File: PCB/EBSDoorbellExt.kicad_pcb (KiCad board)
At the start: 2 copper layers, 65.8 x 49 mm, 41 parts, among them P1 AC in, P2 Doorbell, Q1 BC846C, SW1 Power, SW2 Test, U1 LM7809ACT, U2 LM555N

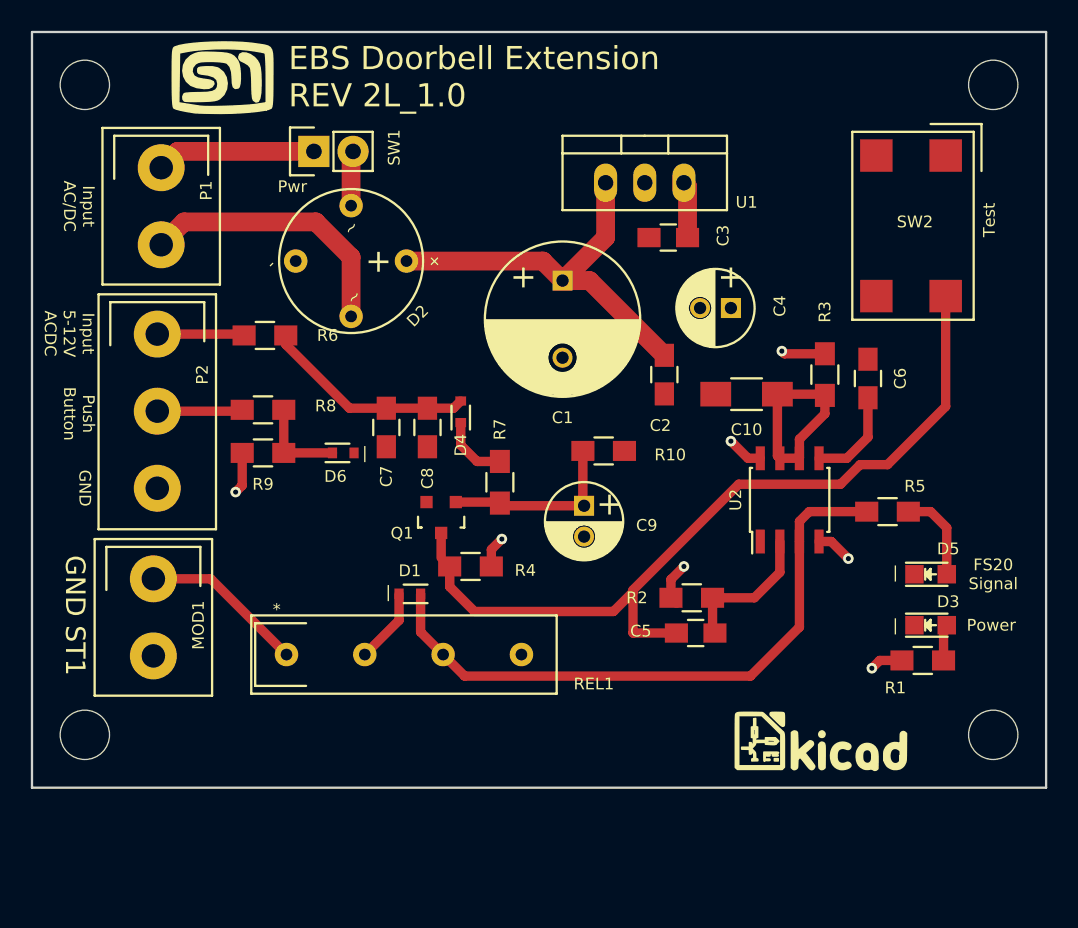
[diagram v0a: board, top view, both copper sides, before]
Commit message: Updated the layout to include the heatsink
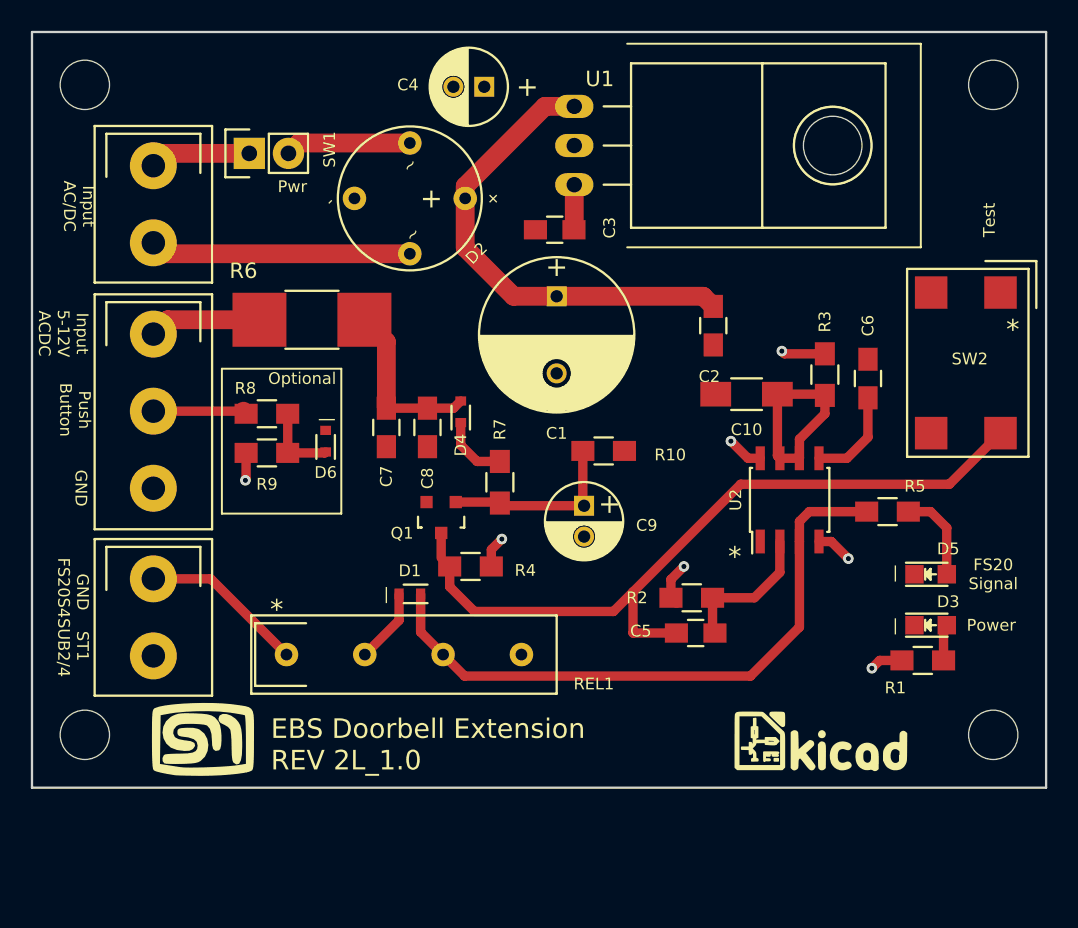
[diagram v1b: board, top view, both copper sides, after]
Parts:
- added REF**: 274_2AB, EBSDoorbellExt-Footprints:274_2AB, F.Cu at (178.3, 74.8)
- R6: footprint Resistors_SMD:R_0805_HandSoldering -> Resistors_SMD:R_1812_HandSoldering
- U1: footprint TO_SOT_Packages_THT:TO-220_Neutral123_Vertical -> TO_SOT_Packages_THT:TO-220_Neutral123_Horizontal
- moved G*** 42.9 mm to (141.2, 113.3)
- moved C4 21.5 mm to (159.5, 71.0)
- moved SW2 9.57 mm to (190.8, 88.9)
- moved C3 7.38 mm to (164.1, 80.3)
- moved D2 5.57 mm to (154.7, 78.2)
- moved U1 5.17 mm to (165.4, 74.8), turned to 270 degrees
- moved C2 4.49 mm to (174.4, 86.5)
- moved SW1 4.19 mm to (144.3, 75.3)
- moved R6 3.21 mm to (148.3, 86.1)
- moved D6 1.37 mm to (149.2, 94.0), turned to 270 degrees
- moved C1 1.09 mm to (164.2, 84.6)
- moved P1 0.52 mm to (138.0, 78.6)
- moved R8 0.36 mm to (145.4, 92.2)
- moved P2 0.25 mm to (138.0, 92.1)
- moved R9 0.25 mm to (145.4, 94.7)
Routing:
- net Net-(D2-Pad2): track 3.57 -> 8.15 mm
- net /~Trigger: track 54.0 -> 49.6 mm
- net Net-(C1-Pad1): track 26.8 -> 30.9 mm
- net /In1: track 10.3 -> 6.56 mm
- net Net-(C7-Pad1): track 13.8 -> 11.3 mm
- net /Vcc: track 21.1 -> 19.4 mm
- net Net-(P2-Pad1): track 5.67 -> 7.27 mm
- net Net-(D6-Pad1): track 5.95 -> 5.03 mm
- net /In2: track 17.7 -> 16.9 mm
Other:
- board text added: "*"
- board text added: "GND ST1 FS20S4SUB2/4"
- board text added: "Optional"
- board text removed: "GND ST1"

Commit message: Added some test points and moved the LEDs help with the casing
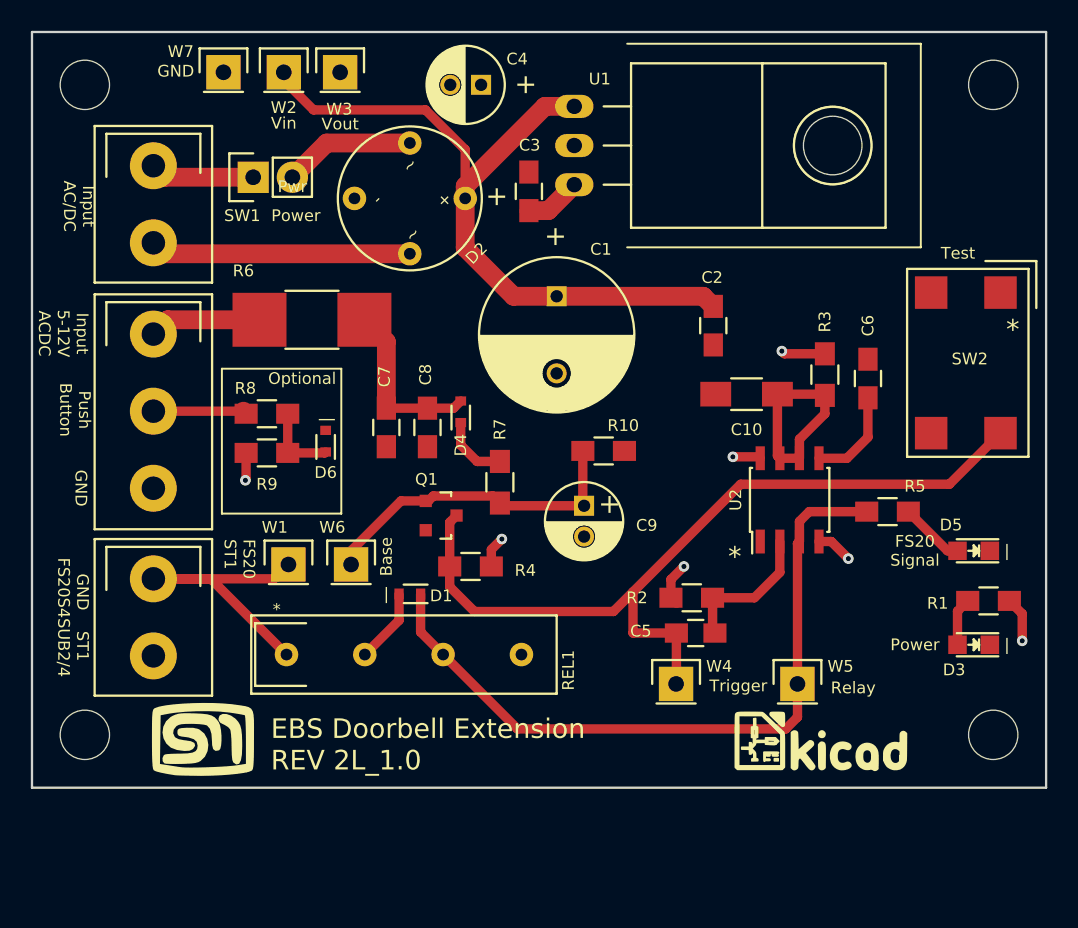
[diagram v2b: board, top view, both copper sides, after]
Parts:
- added W1: FS20_ST1, Pin_Headers:Pin_Header_Straight_1x01, F.Cu at (146.8, 102.0)
- added W2: Vin, Pin_Headers:Pin_Header_Straight_1x01, F.Cu at (146.5, 70.1)
- added W3: Vout, Pin_Headers:Pin_Header_Straight_1x01, F.Cu at (150.2, 70.1)
- added W4: Trigger, Pin_Headers:Pin_Header_Straight_1x01, F.Cu at (172.0, 109.7)
- added W5: Relay, Pin_Headers:Pin_Header_Straight_1x01, F.Cu at (179.8, 109.7)
- added W6: Base, Pin_Headers:Pin_Header_Straight_1x01, F.Cu at (150.9, 102.0)
- added W7: GND, Pin_Headers:Pin_Header_Straight_1x01, F.Cu at (142.6, 70.1)
- U1: value LM7809ACT -> LM7812CT
- moved R1 5.75 mm to (192.2, 104.3), turned to 180 degrees
- moved D5 3.18 mm to (191.3, 101.1), turned to 180 degrees
- moved D3 3.07 mm to (191.3, 107.2), turned to 180 degrees
- moved C3 3.00 mm to (162.4, 77.8), turned to 90 degrees
- moved SW1 1.57 mm to (144.5, 76.9)
- moved C4 0.24 mm to (159.3, 70.9)
- moved Q1 0.13 mm to (156.7, 98.8), turned to 270 degrees
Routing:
- net Net-(C1-Pad1): track 30.9 -> 48.2 mm
- net Net-(C9-Pad1): track 12.0 -> 21.4 mm
- net Net-(MOD1-Pad1): track 10.7 -> 19.8 mm
- net /FS20_Sig: track 41.0 -> 47.2 mm
- net /~Trigger: track 49.6 -> 54.8 mm
- net Net-(D5-Pad2): track 5.94 -> 4.24 mm
- net /Vcc: track 19.4 -> 20.4 mm
- net Net-(D3-Pad2): track 2.37 -> 3.12 mm
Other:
- rule pad_to_mask_clearance: 0.2 -> 0
- board text added: "Base"
- board text added: "FS20 ST1"
- board text added: "Relay"
- board text added: "Trigger"
- board text added: "Vin"
- board text added: "Vout"

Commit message: Changed the layout to use an Optocoupler instead of a relay and generated Gerbers
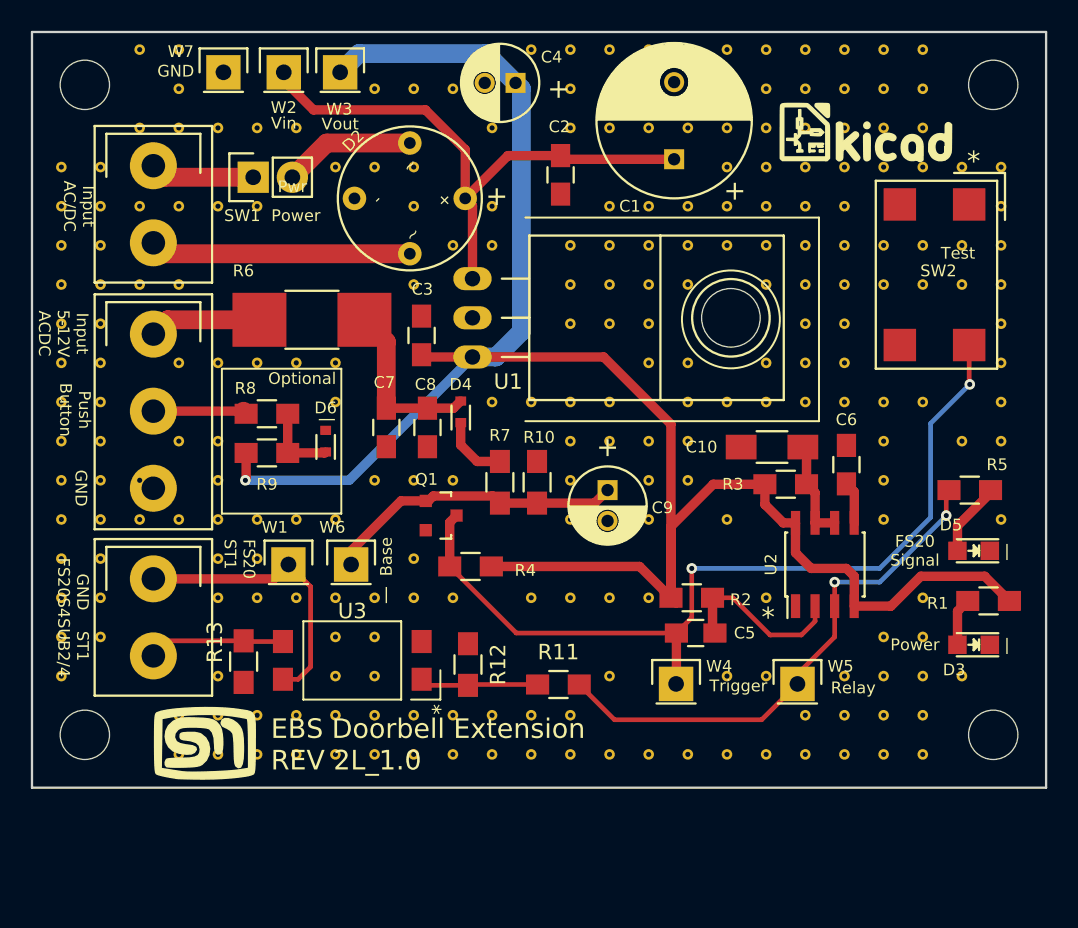
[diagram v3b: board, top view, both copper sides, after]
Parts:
- removed D1: 1N4148W, Diodes_SMD:SOD-523
- removed REL1: MES1A12, EBSDoorbellExt-Footprints:MES1A12
- added R11: 1kΩ, Resistors_SMD:R_0805_HandSoldering, F.Cu at (164.3, 109.8)
- added R12: 10kΩ, Resistors_SMD:R_0805_HandSoldering, F.Cu at (158.5, 108.5)
- added R13: NOPOP, Resistors_SMD:R_0805_HandSoldering, F.Cu at (143.9, 108.3)
- added ST**1012: Stitch_VIA, EBSDoorbellExt-Footprints:Stitch_VIA, F.Cu at (154.9, 96.5)
- added ST**1014: Stitch_VIA, EBSDoorbellExt-Footprints:Stitch_VIA, F.Cu at (154.9, 101.6)
- added ST**1015: Stitch_VIA, EBSDoorbellExt-Footprints:Stitch_VIA, F.Cu at (154.9, 104.1)
- added ST**1018: Stitch_VIA, EBSDoorbellExt-Footprints:Stitch_VIA, F.Cu at (154.9, 111.8)
- added ST**1019: Stitch_VIA, EBSDoorbellExt-Footprints:Stitch_VIA, F.Cu at (154.9, 114.3)
- added ST**102: Stitch_VIA, EBSDoorbellExt-Footprints:Stitch_VIA, F.Cu at (154.9, 71.1)
- added ST**104: Stitch_VIA, EBSDoorbellExt-Footprints:Stitch_VIA, F.Cu at (154.9, 76.2)
- added ST**105: Stitch_VIA, EBSDoorbellExt-Footprints:Stitch_VIA, F.Cu at (154.9, 78.7)
- added ST**107: Stitch_VIA, EBSDoorbellExt-Footprints:Stitch_VIA, F.Cu at (154.9, 83.8)
- added ST**110: Stitch_VIA, EBSDoorbellExt-Footprints:Stitch_VIA, F.Cu at (132.1, 91.4)
- added ST**111: Stitch_VIA, EBSDoorbellExt-Footprints:Stitch_VIA, F.Cu at (132.1, 94.0)
- added ST**1112: Stitch_VIA, EBSDoorbellExt-Footprints:Stitch_VIA, F.Cu at (157.5, 96.5)
- added ST**1115: Stitch_VIA, EBSDoorbellExt-Footprints:Stitch_VIA, F.Cu at (157.5, 104.1)
- added ST**1118: Stitch_VIA, EBSDoorbellExt-Footprints:Stitch_VIA, F.Cu at (157.5, 111.8)
- added ST**1119: Stitch_VIA, EBSDoorbellExt-Footprints:Stitch_VIA, F.Cu at (157.5, 114.3)
- added ST**112: Stitch_VIA, EBSDoorbellExt-Footprints:Stitch_VIA, F.Cu at (132.1, 96.5)
- added ST**112: Stitch_VIA, EBSDoorbellExt-Footprints:Stitch_VIA, F.Cu at (157.5, 71.1)
- added ST**113: Stitch_VIA, EBSDoorbellExt-Footprints:Stitch_VIA, F.Cu at (132.1, 99.1)
- added ST**114: Stitch_VIA, EBSDoorbellExt-Footprints:Stitch_VIA, F.Cu at (132.1, 101.6)
- added ST**115: Stitch_VIA, EBSDoorbellExt-Footprints:Stitch_VIA, F.Cu at (132.1, 104.1)
- added ST**116: Stitch_VIA, EBSDoorbellExt-Footprints:Stitch_VIA, F.Cu at (132.1, 106.7)
- added ST**116: Stitch_VIA, EBSDoorbellExt-Footprints:Stitch_VIA, F.Cu at (157.5, 81.3)
- added ST**117: Stitch_VIA, EBSDoorbellExt-Footprints:Stitch_VIA, F.Cu at (132.1, 109.2)
- added ST**1210: Stitch_VIA, EBSDoorbellExt-Footprints:Stitch_VIA, F.Cu at (160.0, 91.4)
- added ST**1218: Stitch_VIA, EBSDoorbellExt-Footprints:Stitch_VIA, F.Cu at (160.0, 111.8)
- added ST**1219: Stitch_VIA, EBSDoorbellExt-Footprints:Stitch_VIA, F.Cu at (160.0, 114.3)
- added ST**123: Stitch_VIA, EBSDoorbellExt-Footprints:Stitch_VIA, F.Cu at (160.0, 73.7)
- added ST**125: Stitch_VIA, EBSDoorbellExt-Footprints:Stitch_VIA, F.Cu at (160.0, 78.7)
- added ST**126: Stitch_VIA, EBSDoorbellExt-Footprints:Stitch_VIA, F.Cu at (160.0, 81.3)
- added ST**131: Stitch_VIA, EBSDoorbellExt-Footprints:Stitch_VIA, F.Cu at (162.6, 68.6)
- added ST**1310: Stitch_VIA, EBSDoorbellExt-Footprints:Stitch_VIA, F.Cu at (162.6, 91.4)
- added ST**1315: Stitch_VIA, EBSDoorbellExt-Footprints:Stitch_VIA, F.Cu at (162.6, 104.1)
- added ST**1318: Stitch_VIA, EBSDoorbellExt-Footprints:Stitch_VIA, F.Cu at (162.6, 111.8)
- added ST**1319: Stitch_VIA, EBSDoorbellExt-Footprints:Stitch_VIA, F.Cu at (162.6, 114.3)
- added ST**14: Stitch_VIA, EBSDoorbellExt-Footprints:Stitch_VIA, F.Cu at (132.1, 76.2)
- added ST**141: Stitch_VIA, EBSDoorbellExt-Footprints:Stitch_VIA, F.Cu at (165.1, 68.6)
- added ST**1410: Stitch_VIA, EBSDoorbellExt-Footprints:Stitch_VIA, F.Cu at (165.1, 91.4)
- added ST**1411: Stitch_VIA, EBSDoorbellExt-Footprints:Stitch_VIA, F.Cu at (165.1, 94.0)
- added ST**1412: Stitch_VIA, EBSDoorbellExt-Footprints:Stitch_VIA, F.Cu at (165.1, 96.5)
- added ST**1413: Stitch_VIA, EBSDoorbellExt-Footprints:Stitch_VIA, F.Cu at (165.1, 99.1)
- added ST**1415: Stitch_VIA, EBSDoorbellExt-Footprints:Stitch_VIA, F.Cu at (165.1, 104.1)
- added ST**1418: Stitch_VIA, EBSDoorbellExt-Footprints:Stitch_VIA, F.Cu at (165.1, 111.8)
- added ST**1419: Stitch_VIA, EBSDoorbellExt-Footprints:Stitch_VIA, F.Cu at (165.1, 114.3)
- added ST**142: Stitch_VIA, EBSDoorbellExt-Footprints:Stitch_VIA, F.Cu at (165.1, 71.1)
- added ST**143: Stitch_VIA, EBSDoorbellExt-Footprints:Stitch_VIA, F.Cu at (165.1, 73.7)
- added ST**146: Stitch_VIA, EBSDoorbellExt-Footprints:Stitch_VIA, F.Cu at (165.1, 81.3)
- added ST**147: Stitch_VIA, EBSDoorbellExt-Footprints:Stitch_VIA, F.Cu at (165.1, 83.8)
- added ST**148: Stitch_VIA, EBSDoorbellExt-Footprints:Stitch_VIA, F.Cu at (165.1, 86.4)
- added ST**15: Stitch_VIA, EBSDoorbellExt-Footprints:Stitch_VIA, F.Cu at (132.1, 78.7)
- added ST**151: Stitch_VIA, EBSDoorbellExt-Footprints:Stitch_VIA, F.Cu at (167.6, 68.6)
- added ST**1510: Stitch_VIA, EBSDoorbellExt-Footprints:Stitch_VIA, F.Cu at (167.6, 91.4)
- added ST**1511: Stitch_VIA, EBSDoorbellExt-Footprints:Stitch_VIA, F.Cu at (167.6, 94.0)
- added ST**1513: Stitch_VIA, EBSDoorbellExt-Footprints:Stitch_VIA, F.Cu at (167.6, 99.1)
- added ST**1515: Stitch_VIA, EBSDoorbellExt-Footprints:Stitch_VIA, F.Cu at (167.6, 104.1)
- added ST**1517: Stitch_VIA, EBSDoorbellExt-Footprints:Stitch_VIA, F.Cu at (167.6, 109.2)
- added ST**1519: Stitch_VIA, EBSDoorbellExt-Footprints:Stitch_VIA, F.Cu at (167.6, 114.3)
- added ST**152: Stitch_VIA, EBSDoorbellExt-Footprints:Stitch_VIA, F.Cu at (167.6, 71.1)
- added ST**153: Stitch_VIA, EBSDoorbellExt-Footprints:Stitch_VIA, F.Cu at (167.6, 73.7)
- added ST**155: Stitch_VIA, EBSDoorbellExt-Footprints:Stitch_VIA, F.Cu at (167.6, 78.7)
- added ST**156: Stitch_VIA, EBSDoorbellExt-Footprints:Stitch_VIA, F.Cu at (167.6, 81.3)
- added ST**157: Stitch_VIA, EBSDoorbellExt-Footprints:Stitch_VIA, F.Cu at (167.6, 83.8)
- added ST**158: Stitch_VIA, EBSDoorbellExt-Footprints:Stitch_VIA, F.Cu at (167.6, 86.4)
- added ST**16: Stitch_VIA, EBSDoorbellExt-Footprints:Stitch_VIA, F.Cu at (132.1, 81.3)
- added ST**161: Stitch_VIA, EBSDoorbellExt-Footprints:Stitch_VIA, F.Cu at (170.2, 68.6)
- added ST**1611: Stitch_VIA, EBSDoorbellExt-Footprints:Stitch_VIA, F.Cu at (170.2, 94.0)
- added ST**1612: Stitch_VIA, EBSDoorbellExt-Footprints:Stitch_VIA, F.Cu at (170.2, 96.5)
- added ST**1613: Stitch_VIA, EBSDoorbellExt-Footprints:Stitch_VIA, F.Cu at (170.2, 99.1)
- added ST**1615: Stitch_VIA, EBSDoorbellExt-Footprints:Stitch_VIA, F.Cu at (170.2, 104.1)
- added ST**1619: Stitch_VIA, EBSDoorbellExt-Footprints:Stitch_VIA, F.Cu at (170.2, 114.3)
- added ST**162: Stitch_VIA, EBSDoorbellExt-Footprints:Stitch_VIA, F.Cu at (170.2, 71.1)
- added ST**163: Stitch_VIA, EBSDoorbellExt-Footprints:Stitch_VIA, F.Cu at (170.2, 73.7)
- added ST**165: Stitch_VIA, EBSDoorbellExt-Footprints:Stitch_VIA, F.Cu at (170.2, 78.7)
- added ST**166: Stitch_VIA, EBSDoorbellExt-Footprints:Stitch_VIA, F.Cu at (170.2, 81.3)
- added ST**167: Stitch_VIA, EBSDoorbellExt-Footprints:Stitch_VIA, F.Cu at (170.2, 83.8)
- added ST**168: Stitch_VIA, EBSDoorbellExt-Footprints:Stitch_VIA, F.Cu at (170.2, 86.4)
- added ST**169: Stitch_VIA, EBSDoorbellExt-Footprints:Stitch_VIA, F.Cu at (170.2, 88.9)
- added ST**17: Stitch_VIA, EBSDoorbellExt-Footprints:Stitch_VIA, F.Cu at (132.1, 83.8)
- added ST**171: Stitch_VIA, EBSDoorbellExt-Footprints:Stitch_VIA, F.Cu at (172.7, 68.6)
- added ST**1710: Stitch_VIA, EBSDoorbellExt-Footprints:Stitch_VIA, F.Cu at (172.7, 91.4)
- added ST**1711: Stitch_VIA, EBSDoorbellExt-Footprints:Stitch_VIA, F.Cu at (172.7, 94.0)
- added ST**1712: Stitch_VIA, EBSDoorbellExt-Footprints:Stitch_VIA, F.Cu at (172.7, 96.5)
- added ST**1719: Stitch_VIA, EBSDoorbellExt-Footprints:Stitch_VIA, F.Cu at (172.7, 114.3)
- added ST**173: Stitch_VIA, EBSDoorbellExt-Footprints:Stitch_VIA, F.Cu at (172.7, 73.7)
- added ST**175: Stitch_VIA, EBSDoorbellExt-Footprints:Stitch_VIA, F.Cu at (172.7, 78.7)
- added ST**176: Stitch_VIA, EBSDoorbellExt-Footprints:Stitch_VIA, F.Cu at (172.7, 81.3)
- added ST**177: Stitch_VIA, EBSDoorbellExt-Footprints:Stitch_VIA, F.Cu at (172.7, 83.8)
- added ST**179: Stitch_VIA, EBSDoorbellExt-Footprints:Stitch_VIA, F.Cu at (172.7, 88.9)
- added ST**18: Stitch_VIA, EBSDoorbellExt-Footprints:Stitch_VIA, F.Cu at (132.1, 86.4)
- added ST**181: Stitch_VIA, EBSDoorbellExt-Footprints:Stitch_VIA, F.Cu at (175.3, 68.6)
- added ST**1810: Stitch_VIA, EBSDoorbellExt-Footprints:Stitch_VIA, F.Cu at (175.3, 91.4)
- added ST**1813: Stitch_VIA, EBSDoorbellExt-Footprints:Stitch_VIA, F.Cu at (175.3, 99.1)
- added ST**1817: Stitch_VIA, EBSDoorbellExt-Footprints:Stitch_VIA, F.Cu at (175.3, 109.2)
- added ST**1819: Stitch_VIA, EBSDoorbellExt-Footprints:Stitch_VIA, F.Cu at (175.3, 114.3)
- added ST**182: Stitch_VIA, EBSDoorbellExt-Footprints:Stitch_VIA, F.Cu at (175.3, 71.1)
- added ST**183: Stitch_VIA, EBSDoorbellExt-Footprints:Stitch_VIA, F.Cu at (175.3, 73.7)
- added ST**184: Stitch_VIA, EBSDoorbellExt-Footprints:Stitch_VIA, F.Cu at (175.3, 76.2)
- added ST**185: Stitch_VIA, EBSDoorbellExt-Footprints:Stitch_VIA, F.Cu at (175.3, 78.7)
- added ST**186: Stitch_VIA, EBSDoorbellExt-Footprints:Stitch_VIA, F.Cu at (175.3, 81.3)
- added ST**19: Stitch_VIA, EBSDoorbellExt-Footprints:Stitch_VIA, F.Cu at (132.1, 88.9)
- added ST**191: Stitch_VIA, EBSDoorbellExt-Footprints:Stitch_VIA, F.Cu at (177.8, 68.6)
- added ST**1910: Stitch_VIA, EBSDoorbellExt-Footprints:Stitch_VIA, F.Cu at (177.8, 91.4)
- added ST**1915: Stitch_VIA, EBSDoorbellExt-Footprints:Stitch_VIA, F.Cu at (177.8, 104.1)
- added ST**1917: Stitch_VIA, EBSDoorbellExt-Footprints:Stitch_VIA, F.Cu at (177.8, 109.2)
- added ST**1919: Stitch_VIA, EBSDoorbellExt-Footprints:Stitch_VIA, F.Cu at (177.8, 114.3)
- added ST**192: Stitch_VIA, EBSDoorbellExt-Footprints:Stitch_VIA, F.Cu at (177.8, 71.1)
- added ST**193: Stitch_VIA, EBSDoorbellExt-Footprints:Stitch_VIA, F.Cu at (177.8, 73.7)
- added ST**194: Stitch_VIA, EBSDoorbellExt-Footprints:Stitch_VIA, F.Cu at (177.8, 76.2)
- added ST**195: Stitch_VIA, EBSDoorbellExt-Footprints:Stitch_VIA, F.Cu at (177.8, 78.7)
- added ST**196: Stitch_VIA, EBSDoorbellExt-Footprints:Stitch_VIA, F.Cu at (177.8, 81.3)
- added ST**197: Stitch_VIA, EBSDoorbellExt-Footprints:Stitch_VIA, F.Cu at (177.8, 83.8)
- added ST**199: Stitch_VIA, EBSDoorbellExt-Footprints:Stitch_VIA, F.Cu at (177.8, 88.9)
- added ST**201: Stitch_VIA, EBSDoorbellExt-Footprints:Stitch_VIA, F.Cu at (180.3, 68.6)
- added ST**2010: Stitch_VIA, EBSDoorbellExt-Footprints:Stitch_VIA, F.Cu at (180.3, 91.4)
- added ST**2018: Stitch_VIA, EBSDoorbellExt-Footprints:Stitch_VIA, F.Cu at (180.3, 111.8)
- added ST**2019: Stitch_VIA, EBSDoorbellExt-Footprints:Stitch_VIA, F.Cu at (180.3, 114.3)
- added ST**202: Stitch_VIA, EBSDoorbellExt-Footprints:Stitch_VIA, F.Cu at (180.3, 71.1)
- added ST**203: Stitch_VIA, EBSDoorbellExt-Footprints:Stitch_VIA, F.Cu at (180.3, 73.7)
- added ST**204: Stitch_VIA, EBSDoorbellExt-Footprints:Stitch_VIA, F.Cu at (180.3, 76.2)
- added ST**205: Stitch_VIA, EBSDoorbellExt-Footprints:Stitch_VIA, F.Cu at (180.3, 78.7)
- added ST**206: Stitch_VIA, EBSDoorbellExt-Footprints:Stitch_VIA, F.Cu at (180.3, 81.3)
- added ST**207: Stitch_VIA, EBSDoorbellExt-Footprints:Stitch_VIA, F.Cu at (180.3, 83.8)
- added ST**208: Stitch_VIA, EBSDoorbellExt-Footprints:Stitch_VIA, F.Cu at (180.3, 86.4)
- added ST**209: Stitch_VIA, EBSDoorbellExt-Footprints:Stitch_VIA, F.Cu at (180.3, 88.9)
- added ST**210: Stitch_VIA, EBSDoorbellExt-Footprints:Stitch_VIA, F.Cu at (134.6, 91.4)
- added ST**211: Stitch_VIA, EBSDoorbellExt-Footprints:Stitch_VIA, F.Cu at (134.6, 94.0)
- added ST**211: Stitch_VIA, EBSDoorbellExt-Footprints:Stitch_VIA, F.Cu at (182.9, 68.6)
- added ST**2110: Stitch_VIA, EBSDoorbellExt-Footprints:Stitch_VIA, F.Cu at (182.9, 91.4)
- added ST**2117: Stitch_VIA, EBSDoorbellExt-Footprints:Stitch_VIA, F.Cu at (182.9, 109.2)
- added ST**2118: Stitch_VIA, EBSDoorbellExt-Footprints:Stitch_VIA, F.Cu at (182.9, 111.8)
- added ST**2119: Stitch_VIA, EBSDoorbellExt-Footprints:Stitch_VIA, F.Cu at (182.9, 114.3)
- added ST**212: Stitch_VIA, EBSDoorbellExt-Footprints:Stitch_VIA, F.Cu at (134.6, 96.5)
- added ST**212: Stitch_VIA, EBSDoorbellExt-Footprints:Stitch_VIA, F.Cu at (182.9, 71.1)
- added ST**213: Stitch_VIA, EBSDoorbellExt-Footprints:Stitch_VIA, F.Cu at (134.6, 99.1)
- added ST**213: Stitch_VIA, EBSDoorbellExt-Footprints:Stitch_VIA, F.Cu at (182.9, 73.7)
- added ST**214: Stitch_VIA, EBSDoorbellExt-Footprints:Stitch_VIA, F.Cu at (134.6, 101.6)
- added ST**214: Stitch_VIA, EBSDoorbellExt-Footprints:Stitch_VIA, F.Cu at (182.9, 76.2)
- added ST**215: Stitch_VIA, EBSDoorbellExt-Footprints:Stitch_VIA, F.Cu at (134.6, 104.1)
- added ST**215: Stitch_VIA, EBSDoorbellExt-Footprints:Stitch_VIA, F.Cu at (182.9, 78.7)
- added ST**216: Stitch_VIA, EBSDoorbellExt-Footprints:Stitch_VIA, F.Cu at (134.6, 106.7)
- added ST**216: Stitch_VIA, EBSDoorbellExt-Footprints:Stitch_VIA, F.Cu at (182.9, 81.3)
- added ST**217: Stitch_VIA, EBSDoorbellExt-Footprints:Stitch_VIA, F.Cu at (182.9, 83.8)
- added ST**218: Stitch_VIA, EBSDoorbellExt-Footprints:Stitch_VIA, F.Cu at (182.9, 86.4)
- added ST**219: Stitch_VIA, EBSDoorbellExt-Footprints:Stitch_VIA, F.Cu at (182.9, 88.9)
- added ST**221: Stitch_VIA, EBSDoorbellExt-Footprints:Stitch_VIA, F.Cu at (185.4, 68.6)
- added ST**2210: Stitch_VIA, EBSDoorbellExt-Footprints:Stitch_VIA, F.Cu at (185.4, 91.4)
- added ST**2211: Stitch_VIA, EBSDoorbellExt-Footprints:Stitch_VIA, F.Cu at (185.4, 94.0)
- added ST**2212: Stitch_VIA, EBSDoorbellExt-Footprints:Stitch_VIA, F.Cu at (185.4, 96.5)
- added ST**2213: Stitch_VIA, EBSDoorbellExt-Footprints:Stitch_VIA, F.Cu at (185.4, 99.1)
- added ST**2216: Stitch_VIA, EBSDoorbellExt-Footprints:Stitch_VIA, F.Cu at (185.4, 106.7)
- added ST**2217: Stitch_VIA, EBSDoorbellExt-Footprints:Stitch_VIA, F.Cu at (185.4, 109.2)
- added ST**2218: Stitch_VIA, EBSDoorbellExt-Footprints:Stitch_VIA, F.Cu at (185.4, 111.8)
- added ST**2219: Stitch_VIA, EBSDoorbellExt-Footprints:Stitch_VIA, F.Cu at (185.4, 114.3)
- added ST**222: Stitch_VIA, EBSDoorbellExt-Footprints:Stitch_VIA, F.Cu at (185.4, 71.1)
- added ST**223: Stitch_VIA, EBSDoorbellExt-Footprints:Stitch_VIA, F.Cu at (185.4, 73.7)
- added ST**224: Stitch_VIA, EBSDoorbellExt-Footprints:Stitch_VIA, F.Cu at (185.4, 76.2)
- added ST**226: Stitch_VIA, EBSDoorbellExt-Footprints:Stitch_VIA, F.Cu at (185.4, 81.3)
- added ST**227: Stitch_VIA, EBSDoorbellExt-Footprints:Stitch_VIA, F.Cu at (185.4, 83.8)
- added ST**231: Stitch_VIA, EBSDoorbellExt-Footprints:Stitch_VIA, F.Cu at (188.0, 68.6)
- added ST**2310: Stitch_VIA, EBSDoorbellExt-Footprints:Stitch_VIA, F.Cu at (188.0, 91.4)
- added ST**2315: Stitch_VIA, EBSDoorbellExt-Footprints:Stitch_VIA, F.Cu at (188.0, 104.1)
- added ST**2316: Stitch_VIA, EBSDoorbellExt-Footprints:Stitch_VIA, F.Cu at (188.0, 106.7)
- added ST**2317: Stitch_VIA, EBSDoorbellExt-Footprints:Stitch_VIA, F.Cu at (188.0, 109.2)
- added ST**2318: Stitch_VIA, EBSDoorbellExt-Footprints:Stitch_VIA, F.Cu at (188.0, 111.8)
- added ST**2319: Stitch_VIA, EBSDoorbellExt-Footprints:Stitch_VIA, F.Cu at (188.0, 114.3)
- added ST**232: Stitch_VIA, EBSDoorbellExt-Footprints:Stitch_VIA, F.Cu at (188.0, 71.1)
- added ST**233: Stitch_VIA, EBSDoorbellExt-Footprints:Stitch_VIA, F.Cu at (188.0, 73.7)
- added ST**234: Stitch_VIA, EBSDoorbellExt-Footprints:Stitch_VIA, F.Cu at (188.0, 76.2)
- added ST**236: Stitch_VIA, EBSDoorbellExt-Footprints:Stitch_VIA, F.Cu at (188.0, 81.3)
- added ST**237: Stitch_VIA, EBSDoorbellExt-Footprints:Stitch_VIA, F.Cu at (188.0, 83.8)
- added ST**24: Stitch_VIA, EBSDoorbellExt-Footprints:Stitch_VIA, F.Cu at (134.6, 76.2)
- added ST**2411: Stitch_VIA, EBSDoorbellExt-Footprints:Stitch_VIA, F.Cu at (190.5, 94.0)
- added ST**2417: Stitch_VIA, EBSDoorbellExt-Footprints:Stitch_VIA, F.Cu at (190.5, 109.2)
- added ST**244: Stitch_VIA, EBSDoorbellExt-Footprints:Stitch_VIA, F.Cu at (190.5, 76.2)
- added ST**246: Stitch_VIA, EBSDoorbellExt-Footprints:Stitch_VIA, F.Cu at (190.5, 81.3)
- added ST**247: Stitch_VIA, EBSDoorbellExt-Footprints:Stitch_VIA, F.Cu at (190.5, 83.8)
- added ST**25: Stitch_VIA, EBSDoorbellExt-Footprints:Stitch_VIA, F.Cu at (134.6, 78.7)
- added ST**2510: Stitch_VIA, EBSDoorbellExt-Footprints:Stitch_VIA, F.Cu at (193.0, 91.4)
- added ST**2511: Stitch_VIA, EBSDoorbellExt-Footprints:Stitch_VIA, F.Cu at (193.0, 94.0)
- added ST**2513: Stitch_VIA, EBSDoorbellExt-Footprints:Stitch_VIA, F.Cu at (193.0, 99.1)
- added ST**254: Stitch_VIA, EBSDoorbellExt-Footprints:Stitch_VIA, F.Cu at (193.0, 76.2)
- added ST**255: Stitch_VIA, EBSDoorbellExt-Footprints:Stitch_VIA, F.Cu at (193.0, 78.7)
- added ST**256: Stitch_VIA, EBSDoorbellExt-Footprints:Stitch_VIA, F.Cu at (193.0, 81.3)
- added ST**257: Stitch_VIA, EBSDoorbellExt-Footprints:Stitch_VIA, F.Cu at (193.0, 83.8)
- added ST**258: Stitch_VIA, EBSDoorbellExt-Footprints:Stitch_VIA, F.Cu at (193.0, 86.4)
- added ST**259: Stitch_VIA, EBSDoorbellExt-Footprints:Stitch_VIA, F.Cu at (193.0, 88.9)
- added ST**26: Stitch_VIA, EBSDoorbellExt-Footprints:Stitch_VIA, F.Cu at (134.6, 81.3)
- added ST**27: Stitch_VIA, EBSDoorbellExt-Footprints:Stitch_VIA, F.Cu at (134.6, 83.8)
- added ST**28: Stitch_VIA, EBSDoorbellExt-Footprints:Stitch_VIA, F.Cu at (134.6, 86.4)
- added ST**29: Stitch_VIA, EBSDoorbellExt-Footprints:Stitch_VIA, F.Cu at (134.6, 88.9)
- added ST**31: Stitch_VIA, EBSDoorbellExt-Footprints:Stitch_VIA, F.Cu at (137.2, 68.6)
- added ST**312: Stitch_VIA, EBSDoorbellExt-Footprints:Stitch_VIA, F.Cu at (137.2, 96.5)
- added ST**313: Stitch_VIA, EBSDoorbellExt-Footprints:Stitch_VIA, F.Cu at (137.2, 99.1)
- added ST**33: Stitch_VIA, EBSDoorbellExt-Footprints:Stitch_VIA, F.Cu at (137.2, 73.7)
- added ST**35: Stitch_VIA, EBSDoorbellExt-Footprints:Stitch_VIA, F.Cu at (137.2, 78.7)
- added ST**37: Stitch_VIA, EBSDoorbellExt-Footprints:Stitch_VIA, F.Cu at (137.2, 83.8)
- added ST**41: Stitch_VIA, EBSDoorbellExt-Footprints:Stitch_VIA, F.Cu at (139.7, 68.6)
- added ST**411: Stitch_VIA, EBSDoorbellExt-Footprints:Stitch_VIA, F.Cu at (139.7, 94.0)
- added ST**413: Stitch_VIA, EBSDoorbellExt-Footprints:Stitch_VIA, F.Cu at (139.7, 99.1)
- added ST**418: Stitch_VIA, EBSDoorbellExt-Footprints:Stitch_VIA, F.Cu at (139.7, 111.8)
- added ST**419: Stitch_VIA, EBSDoorbellExt-Footprints:Stitch_VIA, F.Cu at (139.7, 114.3)
- added ST**42: Stitch_VIA, EBSDoorbellExt-Footprints:Stitch_VIA, F.Cu at (139.7, 71.1)
- added ST**43: Stitch_VIA, EBSDoorbellExt-Footprints:Stitch_VIA, F.Cu at (139.7, 73.7)
- added ST**45: Stitch_VIA, EBSDoorbellExt-Footprints:Stitch_VIA, F.Cu at (139.7, 78.7)
- added ST**47: Stitch_VIA, EBSDoorbellExt-Footprints:Stitch_VIA, F.Cu at (139.7, 83.8)
- added ST**49: Stitch_VIA, EBSDoorbellExt-Footprints:Stitch_VIA, F.Cu at (139.7, 88.9)
- added ST**511: Stitch_VIA, EBSDoorbellExt-Footprints:Stitch_VIA, F.Cu at (142.2, 94.0)
- added ST**512: Stitch_VIA, EBSDoorbellExt-Footprints:Stitch_VIA, F.Cu at (142.2, 96.5)
- added ST**513: Stitch_VIA, EBSDoorbellExt-Footprints:Stitch_VIA, F.Cu at (142.2, 99.1)
- added ST**514: Stitch_VIA, EBSDoorbellExt-Footprints:Stitch_VIA, F.Cu at (142.2, 101.6)
- added ST**515: Stitch_VIA, EBSDoorbellExt-Footprints:Stitch_VIA, F.Cu at (142.2, 104.1)
- added ST**517: Stitch_VIA, EBSDoorbellExt-Footprints:Stitch_VIA, F.Cu at (142.2, 109.2)
- added ST**518: Stitch_VIA, EBSDoorbellExt-Footprints:Stitch_VIA, F.Cu at (142.2, 111.8)
- added ST**519: Stitch_VIA, EBSDoorbellExt-Footprints:Stitch_VIA, F.Cu at (142.2, 114.3)
- added ST**53: Stitch_VIA, EBSDoorbellExt-Footprints:Stitch_VIA, F.Cu at (142.2, 73.7)
- added ST**55: Stitch_VIA, EBSDoorbellExt-Footprints:Stitch_VIA, F.Cu at (142.2, 78.7)
- added ST**59: Stitch_VIA, EBSDoorbellExt-Footprints:Stitch_VIA, F.Cu at (142.2, 88.9)
- added ST**613: Stitch_VIA, EBSDoorbellExt-Footprints:Stitch_VIA, F.Cu at (144.8, 99.1)
- added ST**614: Stitch_VIA, EBSDoorbellExt-Footprints:Stitch_VIA, F.Cu at (144.8, 101.6)
- added ST**615: Stitch_VIA, EBSDoorbellExt-Footprints:Stitch_VIA, F.Cu at (144.8, 104.1)
- added ST**618: Stitch_VIA, EBSDoorbellExt-Footprints:Stitch_VIA, F.Cu at (144.8, 111.8)
- added ST**619: Stitch_VIA, EBSDoorbellExt-Footprints:Stitch_VIA, F.Cu at (144.8, 114.3)
- added ST**63: Stitch_VIA, EBSDoorbellExt-Footprints:Stitch_VIA, F.Cu at (144.8, 73.7)
- added ST**65: Stitch_VIA, EBSDoorbellExt-Footprints:Stitch_VIA, F.Cu at (144.8, 78.7)
- added ST**69: Stitch_VIA, EBSDoorbellExt-Footprints:Stitch_VIA, F.Cu at (144.8, 88.9)
- added ST**713: Stitch_VIA, EBSDoorbellExt-Footprints:Stitch_VIA, F.Cu at (147.3, 99.1)
- added ST**715: Stitch_VIA, EBSDoorbellExt-Footprints:Stitch_VIA, F.Cu at (147.3, 104.1)
- added ST**718: Stitch_VIA, EBSDoorbellExt-Footprints:Stitch_VIA, F.Cu at (147.3, 111.8)
- added ST**719: Stitch_VIA, EBSDoorbellExt-Footprints:Stitch_VIA, F.Cu at (147.3, 114.3)
- added ST**73: Stitch_VIA, EBSDoorbellExt-Footprints:Stitch_VIA, F.Cu at (147.3, 73.7)
- added ST**79: Stitch_VIA, EBSDoorbellExt-Footprints:Stitch_VIA, F.Cu at (147.3, 88.9)
- added ST**810: Stitch_VIA, EBSDoorbellExt-Footprints:Stitch_VIA, F.Cu at (149.9, 91.4)
- added ST**813: Stitch_VIA, EBSDoorbellExt-Footprints:Stitch_VIA, F.Cu at (149.9, 99.1)
- added ST**815: Stitch_VIA, EBSDoorbellExt-Footprints:Stitch_VIA, F.Cu at (149.9, 104.1)
- added ST**816: Stitch_VIA, EBSDoorbellExt-Footprints:Stitch_VIA, F.Cu at (149.9, 106.7)
- added ST**817: Stitch_VIA, EBSDoorbellExt-Footprints:Stitch_VIA, F.Cu at (149.9, 109.2)
- added ST**818: Stitch_VIA, EBSDoorbellExt-Footprints:Stitch_VIA, F.Cu at (149.9, 111.8)
- added ST**819: Stitch_VIA, EBSDoorbellExt-Footprints:Stitch_VIA, F.Cu at (149.9, 114.3)
- added ST**84: Stitch_VIA, EBSDoorbellExt-Footprints:Stitch_VIA, F.Cu at (149.9, 76.2)
- added ST**89: Stitch_VIA, EBSDoorbellExt-Footprints:Stitch_VIA, F.Cu at (149.9, 88.9)
- added ST**912: Stitch_VIA, EBSDoorbellExt-Footprints:Stitch_VIA, F.Cu at (152.4, 96.5)
- added ST**915: Stitch_VIA, EBSDoorbellExt-Footprints:Stitch_VIA, F.Cu at (152.4, 104.1)
- added ST**916: Stitch_VIA, EBSDoorbellExt-Footprints:Stitch_VIA, F.Cu at (152.4, 106.7)
- added ST**917: Stitch_VIA, EBSDoorbellExt-Footprints:Stitch_VIA, F.Cu at (152.4, 109.2)
- added ST**918: Stitch_VIA, EBSDoorbellExt-Footprints:Stitch_VIA, F.Cu at (152.4, 111.8)
- added ST**919: Stitch_VIA, EBSDoorbellExt-Footprints:Stitch_VIA, F.Cu at (152.4, 114.3)
- added ST**92: Stitch_VIA, EBSDoorbellExt-Footprints:Stitch_VIA, F.Cu at (152.4, 71.1)
- added ST**94: Stitch_VIA, EBSDoorbellExt-Footprints:Stitch_VIA, F.Cu at (152.4, 76.2)
- added U3: LTV-817, EBSDoorbellExt-Footprints:LTV_817, F.Cu at (151.0, 108.2)
- U1: value LM7812CT -> LM7809CT
- moved G*** 39.6 mm to (184.3, 73.9)
- moved C2 13.9 mm to (164.5, 76.7)
- moved U1 13.0 mm to (158.8, 86.0)
- moved C1 11.7 mm to (171.8, 75.7), turned to 90 degrees
- moved C3 11.7 mm to (155.4, 87.1)
- moved REF** 11.6 mm to (175.5, 86.1)
- moved R3 7.55 mm to (179.1, 96.8), turned to 0 degrees
- moved SW2 6.07 mm to (188.7, 83.2)
- moved C6 5.76 mm to (183.0, 95.5)
- moved R5 5.51 mm to (191.0, 97.2)
- moved U2 4.77 mm to (181.6, 102.0)
- moved R10 4.77 mm to (162.9, 96.6), turned to 270 degrees
- moved C10 3.81 mm to (178.2, 94.4)
- moved C4 2.24 mm to (161.5, 70.7)
- moved C9 1.83 mm to (167.5, 97.2)
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- renumbered REF** to REF**11
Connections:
- MOD1 pad 2: GND -> Net-(MOD1-Pad2)
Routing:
- net /Vcc: track 20.4 -> 130.8 mm, vias 7 -> 1
- net /FS20_Sig: track 47.2 -> 34.4 mm, vias 0 -> 2
- net Net-(C1-Pad1): track 48.2 -> 37.5 mm
- net Net-(MOD1-Pad2): track 0.00 -> 8.83 mm
- net Net-(R11-Pad1): track 0.00 -> 7.71 mm
- net Net-(C10-Pad1): track 13.4 -> 6.52 mm
- net GND: track 4.86 -> 0.00 mm
- net Net-(C6-Pad2): track 6.30 -> 2.74 mm
- net /~Trigger: track 54.8 -> 57.1 mm, vias 0 -> 2
- net Net-(C5-Pad1): track 9.40 -> 11.4 mm
- net Net-(C9-Pad1): track 21.4 -> 19.9 mm
- net Net-(MOD1-Pad1): track 19.8 -> 18.5 mm
- net Net-(D5-Pad2): track 4.24 -> 4.83 mm
- added copper zone on B.Cu, net GND
- removed copper zone on B.Cu, net /Vcc

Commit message: Corrected some footprint issues
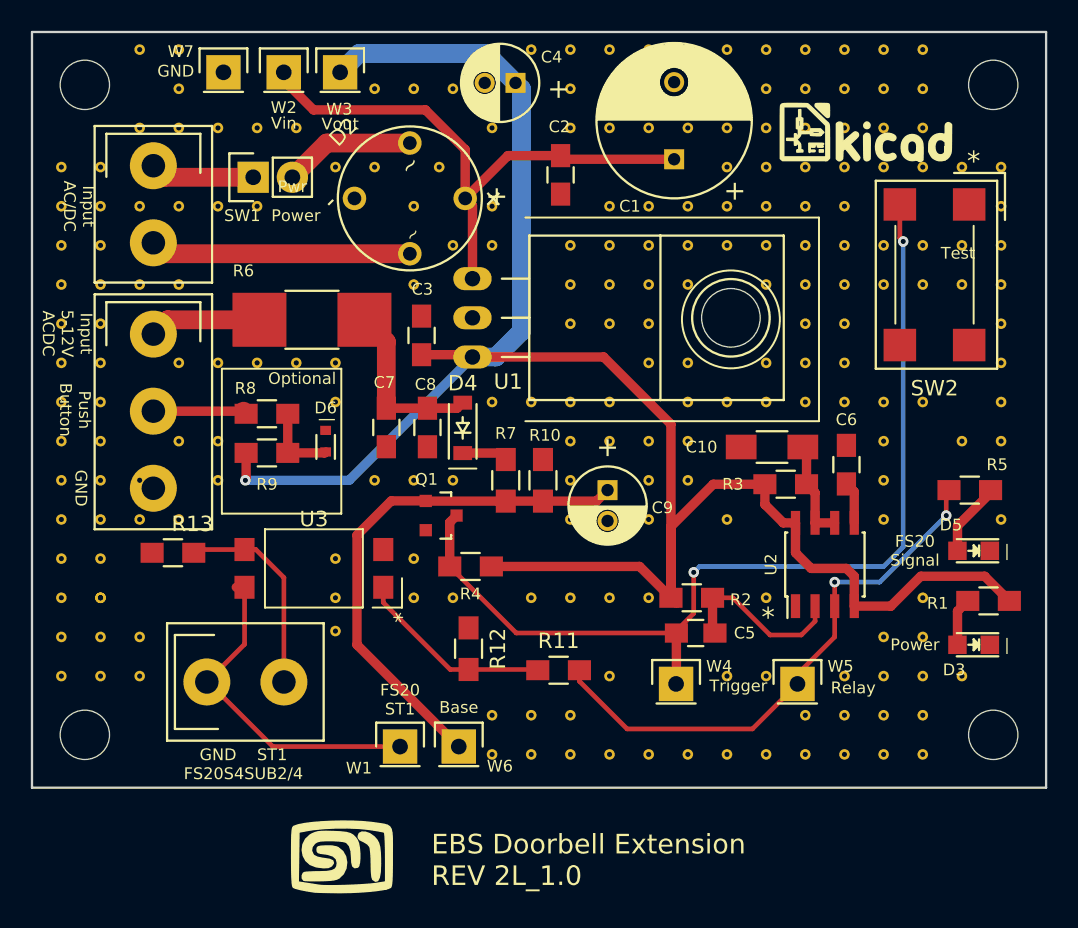
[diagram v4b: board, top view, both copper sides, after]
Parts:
- removed ST**1018, ST**1019, ST**1118, ST**1119, ST**418, ST**419, ST**513, ST**514, ST**515, ST**517, ST**518, ST**519, ST**613, ST**614, ST**615, ST**618, ST**619, ST**713, ST**715, ST**718, ST**719, ST**813, ST**815, ST**816, ST**817, ST**818, ST**819, ST**915, ST**916, ST**917, ST**918, ST**919: Stitch_VIA, EBSDoorbellExt-Footprints:Stitch_VIA
- added ST**211111: Stitch_VIA, EBSDoorbellExt-Footprints:Stitch_VIA, F.Cu at (137.2, 106.7)
- added ST**2112: Stitch_VIA, EBSDoorbellExt-Footprints:Stitch_VIA, F.Cu at (134.6, 104.1)
- added ST**216: Stitch_VIA, EBSDoorbellExt-Footprints:Stitch_VIA, F.Cu at (137.2, 109.2)
- added ST**216: Stitch_VIA, EBSDoorbellExt-Footprints:Stitch_VIA, F.Cu at (134.6, 109.2)
- added ST**21711: Stitch_VIA, EBSDoorbellExt-Footprints:Stitch_VIA, F.Cu at (149.9, 104.1)
- added ST**21711: Stitch_VIA, EBSDoorbellExt-Footprints:Stitch_VIA, F.Cu at (149.9, 101.6)
- added ST**21712: Stitch_VIA, EBSDoorbellExt-Footprints:Stitch_VIA, F.Cu at (149.9, 106.3)
- D4: footprint Diodes_SMD:SOD-523 -> Diodes_SMD:SOD-123
- SW2: value Test -> FSM2JSMAA
- moved W1 13.9 mm to (154.1, 113.8)
- moved W6 13.7 mm to (157.9, 113.8)
- moved G*** 11.5 mm to (150.2, 120.9)
- moved R13 8.42 mm to (139.3, 101.2), turned to 180 degrees
- moved MOD1 7.29 mm to (144.0, 109.6), turned to 0 degrees
- moved U3 6.47 mm to (148.5, 102.2)
- moved ST**104 1.65 mm to (156.6, 76.2)
- moved D4 1.05 mm to (158.1, 93.1), turned to 90 degrees
- moved R12 1.03 mm to (158.5, 107.4)
- moved R11 0.93 mm to (164.3, 108.8)
- moved R10 0.40 mm to (163.3, 96.5)
- moved R7 0.40 mm to (160.9, 96.5)
- renumbered ST**214 to ST**2111
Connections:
- SW2 pad 2: /~Trigger -> Net-(SW2-Pad2)
- SW2 pad 3: (no net) -> /~Trigger
- SW2 pad 4: (no net) -> Net-(SW2-Pad4)
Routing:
- net Net-(C9-Pad1): track 19.9 -> 34.8 mm
- net /~Trigger: track 57.1 -> 64.3 mm
- net Net-(R11-Pad1): track 7.71 -> 12.8 mm
- net Net-(MOD1-Pad2): track 8.83 -> 13.8 mm
- net Net-(MOD1-Pad1): track 18.5 -> 22.0 mm
- net Net-(D4-Pad1): track 4.44 -> 2.97 mm
- net /FS20_Sig: track 34.4 -> 35.7 mm
